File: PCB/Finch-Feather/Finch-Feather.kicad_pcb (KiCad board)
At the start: 4 copper layers, 61 x 22.9 mm, 37 parts, among them M1 STM32WB5MMGH6TR, Q1 DMP3125L-7, SW1 B3U-1000P, T1 20021121-00010C4LF, T2 TSW-112-07-G-S, T3 DX07S016JA1R1500, T4 TSW-116-07-L-S, T5 S2B-PH-SM4-TB(LF)(SN), U1 USBLC6-2P6, U2 TLV75533PDBVR, U3 MCP73831T-2ACI_MC

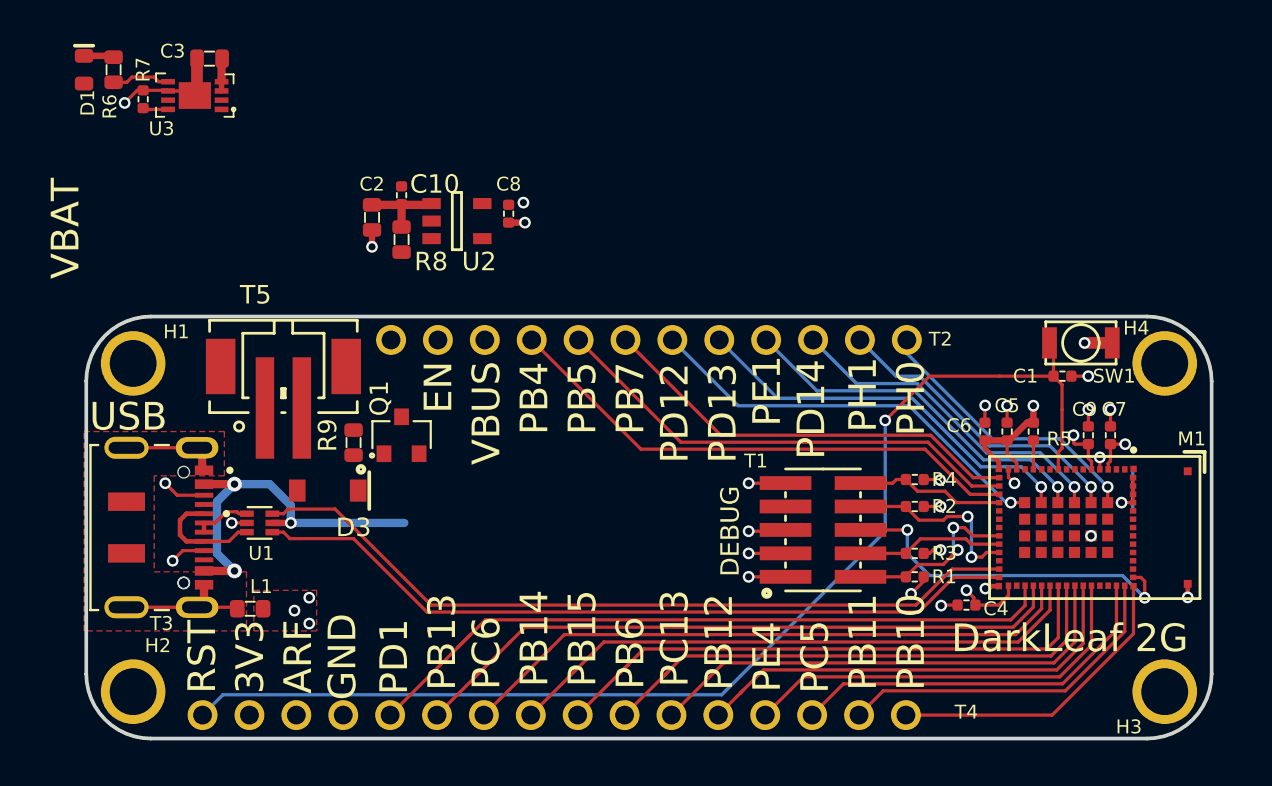
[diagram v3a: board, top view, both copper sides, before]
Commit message: PCB pass COmplete
First true pass of PCB fully complete, with new power switching circuit and regulator enable. Smaller packages selected for pretty much every IC previously used.
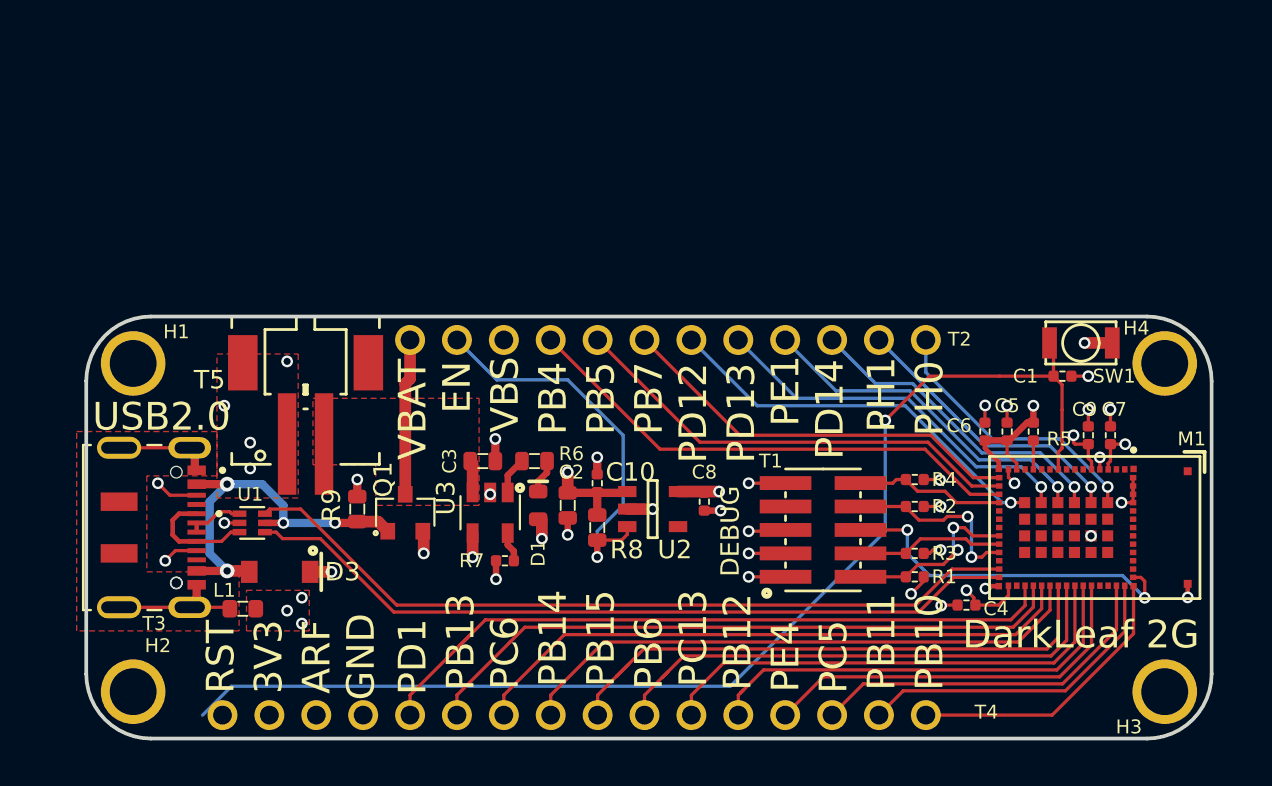
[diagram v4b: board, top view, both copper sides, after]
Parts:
- U3: value MCP73831T-2ACI_MC -> MCP73831T-2ACI_OT; footprint AVR-KiCAD-Lib-ICs:MCP73831T-2ACI-MC -> AVR-KiCAD-Lib-ICs:SOT-23-5
- moved D1 34.1 mm to (144.0, 98.8)
- moved R7 31.8 mm to (142.2, 101.8), turned to 180 degrees
- moved R6 31.1 mm to (143.8, 96.4), turned to 180 degrees
- moved U3 27.7 mm to (141.4, 99.2), turned to 270 degrees
- moved C3 26.3 mm to (141.0, 96.4), turned to 0 degrees
- moved C10 18.9 mm to (147.2, 97.6)
- moved C2 18.9 mm to (145.6, 98.8)
- moved C8 18.9 mm to (153.0, 98.6)
- moved R8 18.9 mm to (147.2, 100.0)
- moved U2 18.9 mm to (150.2, 99.0)
- moved D3 5.11 mm to (130.0, 102.4)
- moved Q1 4.20 mm to (136.8, 99.2)
- moved R9 3.61 mm to (134.2, 99.0)
- moved T5 1.22 mm to (131.4, 92.2)
- moved T4 1.08 mm to (145.9, 110.2)
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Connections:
- U3 pad 1: VCC -> /STAT
- U3 pad 2: VCC -> GND
- U3 pad 4: /VBAT -> VCC
- U3 pad 5: /STAT -> /PROG
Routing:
- net /ENABLE: track 0.00 -> 21.4 mm, vias 0 -> 1
- net VBUS: track 20.4 -> 41.4 mm, vias 3 -> 4
- net /VBAT: track 1.72 -> 10.2 mm
- net VCC: track 4.49 -> 10.3 mm, vias 0 -> 5
- net +3V3: track 21.3 -> 23.4 mm
- net /NRST: track 66.4 -> 64.4 mm
- net /STAT: track 3.37 -> 2.02 mm
- net /PB11: track 18.8 -> 17.7 mm
- net /PB10: track 16.7 -> 15.7 mm
- net /PE4: track 22.5 -> 21.4 mm
- net /PC5: track 20.8 -> 19.7 mm
- net /PD14: track 18.3 -> 17.3 mm
- net /PH1: track 16.7 -> 15.6 mm
- net /PB4: track 28.8 -> 27.8 mm
- net /PD13: track 21.6 -> 20.6 mm
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- added copper zone on F.Cu, net /VBAT
- added copper zone on In2.Cu, net VCC
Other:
- board text added: "USB2.0"
- board text added: "VBS"
- board text removed: "USB"
- board text removed: "VBUS"

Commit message: Heavy PCB Rework
Reworked the Portion of the PCB around the ST RF module, signals re-chosen for 3 GPIOs to make the grounding conform more to the reference design recommendations.
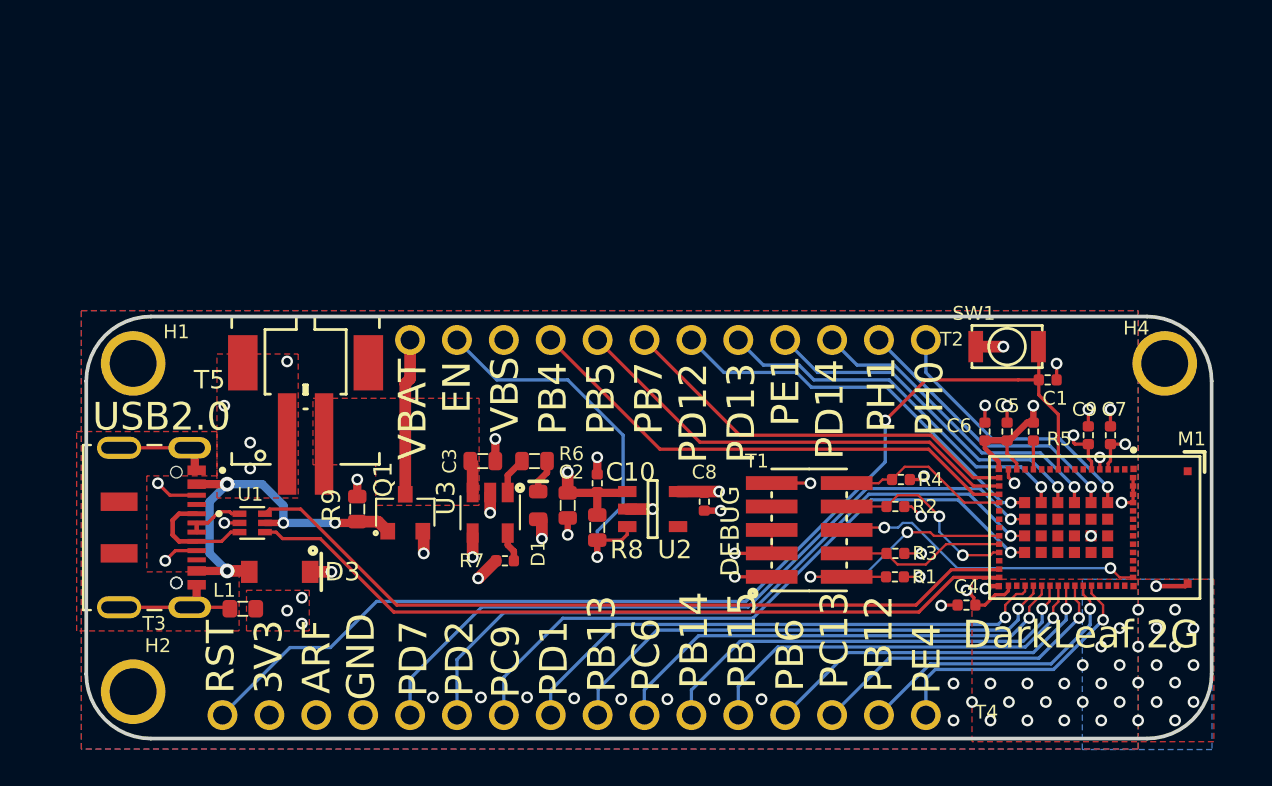
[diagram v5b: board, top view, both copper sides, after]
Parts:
- removed H3: 2.54mm_PLT_Hole, AVR-KiCAD-Lib-Holes_Fasteners:2.54mm_PLT_Hole
- moved SW1 4.00 mm to (169.4, 90.2), turned to 0 degrees
- moved R1 1.08 mm to (163.3, 102.7)
- moved R2 1.05 mm to (163.3, 98.9)
- moved R3 1.05 mm to (163.3, 101.4)
- moved C1 0.82 mm to (171.6, 92.0)
- moved R4 0.75 mm to (163.7, 97.4)
- moved T1 0.75 mm to (158.7, 100.1)
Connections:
- M1 pad 45: /PC5 -> Net-(M1-Pad45)
- M1 pad 67: Net-(M1-Pad67) -> /PD7
- M1 pad 68: Net-(M1-Pad68) -> /PD2
- M1 pad 69: Net-(M1-Pad69) -> /PC9
- T4 pad 10: /PB6 -> /PC6
- T4 pad 11: /PC13 -> /PB14
- T4 pad 12: /PB12 -> /PB15
- T4 pad 13: /PE4 -> /PB6
- T4 pad 14: /PC5 -> /PC13
- T4 pad 15: /PB11 -> /PB12
- T4 pad 16: /PB10 -> /PE4
- T4 pad 5: /PD1 -> /PD7
- T4 pad 6: /PB13 -> /PD2
- T4 pad 7: /PC6 -> /PC9
- T4 pad 8: /PB14 -> /PD1
- T4 pad 9: /PB15 -> /PB13
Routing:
- net /PD7: track 0.00 -> 40.2 mm, vias 0 -> 1
- net /PD2: track 0.00 -> 38.4 mm, vias 0 -> 1
- net /PC9: track 0.00 -> 35.4 mm, vias 0 -> 1
- net /PC5: track 19.7 -> 0.00 mm
- net /PB11: track 17.7 -> 0.00 mm
- net /PB10: track 15.7 -> 0.00 mm
- net /PB6: track 28.6 -> 19.2 mm, vias 0 -> 1
- net /PB15: track 31.1 -> 22.0 mm, vias 0 -> 1
- net /PC13: track 26.1 -> 17.4 mm, vias 0 -> 1
- net /PB12: track 24.3 -> 15.7 mm, vias 0 -> 1
- net /PD1: track 38.4 -> 30.0 mm, vias 0 -> 1
- net /PB14: track 31.6 -> 24.0 mm, vias 0 -> 1
- net /PC6: track 33.4 -> 25.9 mm, vias 0 -> 1
- net /PB13: track 35.5 -> 28.0 mm, vias 0 -> 1
- net /JTAG_SWDIO: track 9.85 -> 16.3 mm
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- added copper zone on B.Cu, net GND
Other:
- net class Default: clearance 0.2 -> 0.127
- rule trace_clearance: 0.2 -> 0.127
- rule trace_min: 0.1778 -> 0.127
- board text added: "PC9"
- board text added: "PD2"
- board text added: "PD7"
- board text removed: "PB10"
- board text removed: "PB11"
- board text removed: "PC5"

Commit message: PCB changes
Adjusted pours, next need to perfrom DRC, syncing for work
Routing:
- net GND: vias 75 -> 76
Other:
- board text added: "BAT"

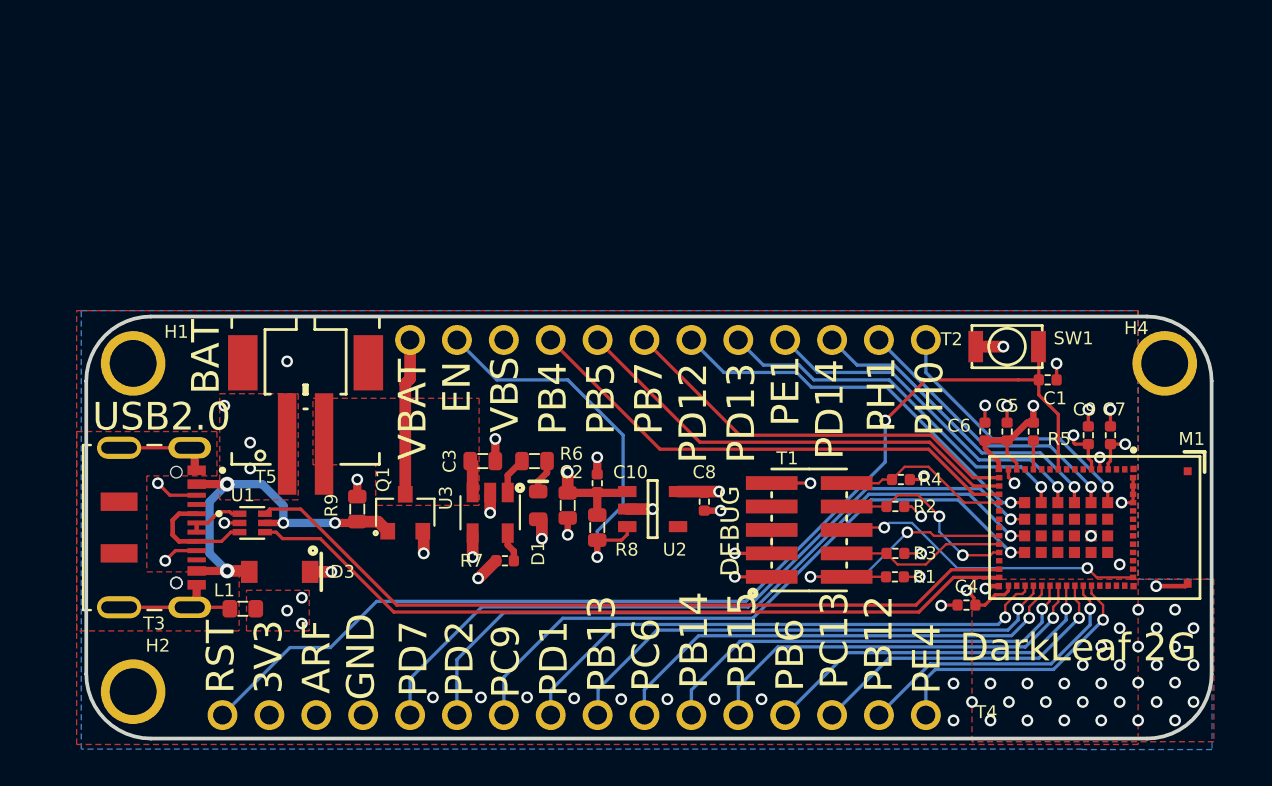
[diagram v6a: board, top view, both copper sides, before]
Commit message: Prefab changes
minor adjustments, removal of screw holes, and additional via stitching
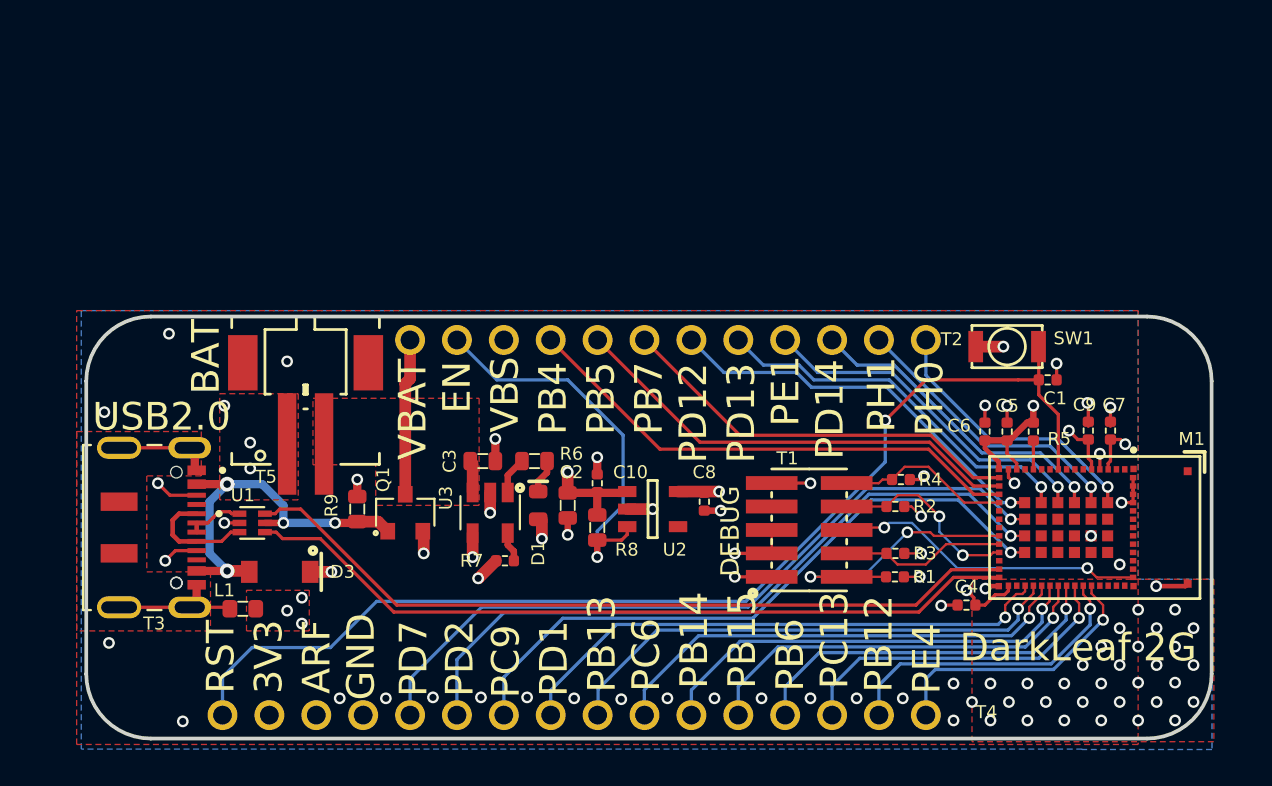
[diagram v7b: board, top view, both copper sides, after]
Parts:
- removed H1, H2, H4: 2.54mm_PLT_Hole, AVR-KiCAD-Lib-Holes_Fasteners:2.54mm_PLT_Hole
- moved C7 0.25 mm to (175.0, 94.8)
- moved C9 0.25 mm to (173.8, 94.8)
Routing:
- net /NRST: track 60.2 -> 61.4 mm
- net /PB12: track 15.7 -> 16.7 mm
- net /PC13: track 17.4 -> 18.3 mm
- net /PB6: track 19.2 -> 20.1 mm
- net GND: track 33.2 -> 33.9 mm, vias 76 -> 85
- net +3V3: track 23.1 -> 23.7 mm
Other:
- rule pad_to_mask_clearance: 0.0508 -> 0

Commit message: KiCAD Project Upadated and Images added
Updated the KiCAD Project to the newest version, restored paths for 3D files for board components. Added 3D rendered images of the board.
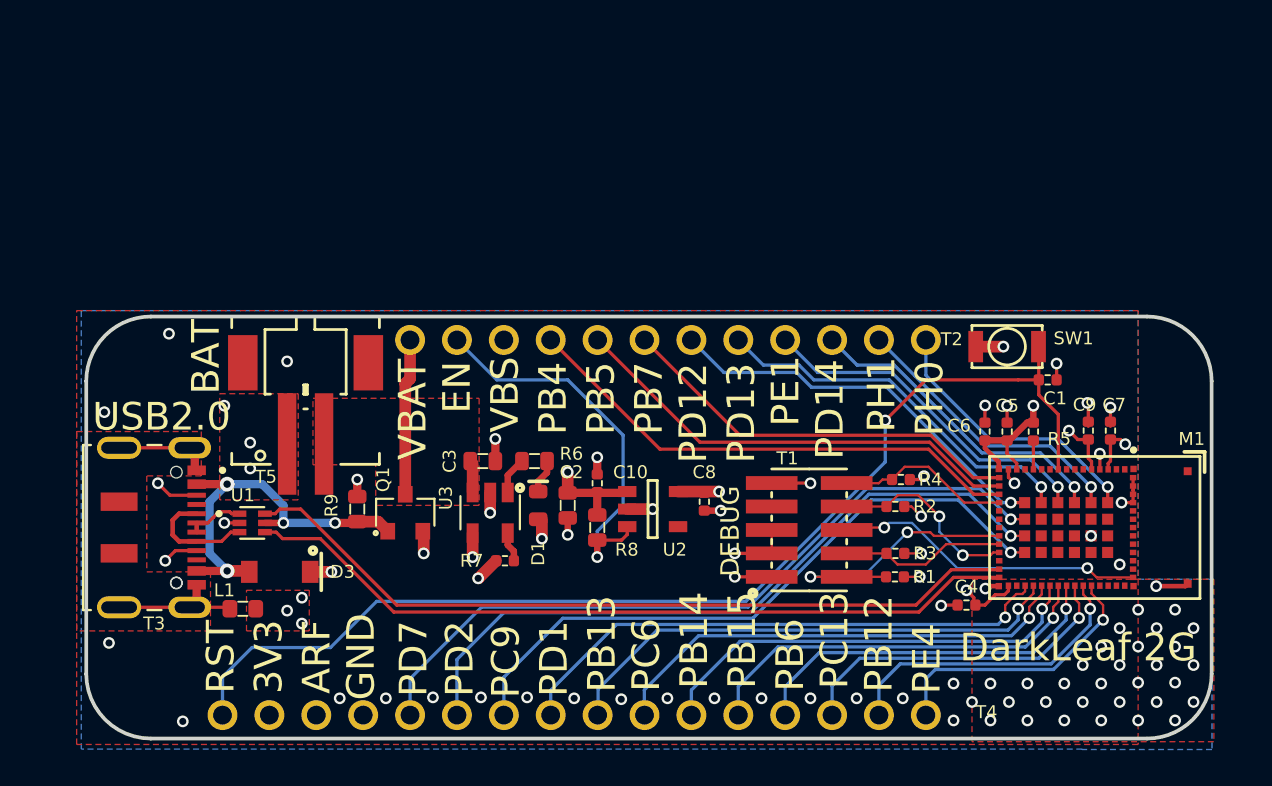
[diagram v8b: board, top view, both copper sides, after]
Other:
- net class Default removed
